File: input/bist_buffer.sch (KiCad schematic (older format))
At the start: 7 parts, among them U9 OPA1679

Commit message: Cleanup to get ready to start board layout. I had to get rid off all the bus signals, since in Kicad busses don't work that way.  Added a couple testpoints; many more needed.
Work on component placement in PCB.  I changed DGND to plain GND and "protective earth" to
"earth" (for chassis ground).  Chassis ground is now connected on the board only via a capacitor.
I had to fix the connector footprint to match the pin numbers on the symbol (there was a case
difference).
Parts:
- U9: footprint digikey-footprints:SOIC-14_W3.9mm -> Package_SO:SOIC-14_3.9x8.7mm_P1.27mm; symbol dk_Linear-Amplifiers-Instrumentation-OP-Amps-Buffer-Amps:LM324ADR -> ilemt_input:opamp_quad
- U9: footprint digikey-footprints:SOIC-14_W3.9mm -> Package_SO:SOIC-14_3.9x8.7mm_P1.27mm; symbol dk_Linear-Amplifiers-Instrumentation-OP-Amps-Buffer-Amps:LM324ADR -> ilemt_input:opamp_quad; Category (none) -> Integrated Circuits (ICs); DK_Datasheet_Link (none) -> http://www.ti.com/general/docs/suppproductinfo.tsp?distId=1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; DK_Detail_Page (none) -> /product-detail/en/texas-instruments/LM324ADR/296-9540-1-ND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; Description IC AUDIO 4 CIRCUIT 14SOIC -> IC OPAMP GP 4 CIRCUIT 14SOIC; Digi-Key_PN (none) -> 296-9540-1-ND; Family (none) -> Linear - Amplifiers - Instrumentation, OP Amps, Buffer Amps; MPN OPA1679IDR -> LM324ADR; Status (none) -> Active
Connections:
- net BIST++: no longer U9.2
- net BIST+-: no longer U9.6
- net BIST-+: no longer U9.9
- net BIST--: no longer U9.13
- new net BIST++_FB: U9.2
- new net BIST+-_FB: U9.6
- new net BIST-+_FB: U9.9
- new net BIST--_FB: U9.13
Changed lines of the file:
@@
 $EndDescr
 $Comp
-L dk_Linear-Amplifiers-Instrumentation-OP-Amps-Buffer-Amps:LM324ADR U9
+L ilemt_input:opamp_quad U9
 U 1 1 5E5A93B1
 P 4900 3100
 F 0 "U9" H 4600 3500 60  0000 C CNN
 F 1 "OPA1679" H 4350 3400 60  0000 L CNN
-F 2 "digikey-footprints:SOIC-14_W3.9mm" H 5100 3300 60  0001 L CNN
+F 2 "Package_SO:SOIC-14_3.9x8.7mm_P1.27mm" H 5100 3300 60  0001 L CNN
 F 3 "http://www.ti.com/general/docs/suppproductinfo.tsp?distId=10&gotoUrl=http%3A%2F%2Fwww.ti.com%2Flit%2Fgpn%2Fopa1679" H 5100 3400 60  0001 L CNN
 F 4 "OPA1679IDR" H 5100 3600 60  0001 L CNN "MPN"
@@
 	4900 3550 5150 3550
 Wire Wire Line
-	4900 2700 4900 2900
-Wire Wire Line
-	4900 3300 4900 3550
+	4900 2700 4900 2800
+Wire Wire Line
+	4900 3400 4900 3550
 $Comp
 L ilemt_input:V+ #PWR041
@@
 	4900 3700 4900 3550
 Connection ~ 4900 3550
-Text HLabel 2600 2150 0    50   Input ~ 0
-BIST_feedback
 Text GLabel 8300 3100 2    50   Input ~ 0
 BIST-+
@@
 Wire Wire Line
 	5550 3100 5200 3100
-Entry Wire Line
-	3900 2150 4000 2250
-Wire Wire Line
-	4000 2250 4000 3000
-Wire Wire Line
-	4000 3000 4600 3000
-Text Label 4050 3000 0    50   ~ 0
-BIST++
-$Comp
-L dk_Linear-Amplifiers-Instrumentation-OP-Amps-Buffer-Amps:LM324ADR U9
+$Comp
+L ilemt_input:opamp_quad U9
 U 2 1 5E5BA1D6
 P 7850 3100
 F 0 "U9" H 7550 3500 60  0000 C CNN
 F 1 "OPA1679" H 7300 3400 60  0000 L CNN
-F 2 "digikey-footprints:SOIC-14_W3.9mm" H 8050 3300 60  0001 L CNN
+F 2 "Package_SO:SOIC-14_3.9x8.7mm_P1.27mm" H 8050 3300 60  0001 L CNN
 F 3 "http://www.ti.com/general/docs/suppproductinfo.tsp?distId=10&gotoUrl=http%3A%2F%2Fwww.ti.com%2Flit%2Fgpn%2Fopa1679" H 8050 3400 60  0001 L CNN
-F 4 "OPA1679IDR" H 8050 3600 60  0001 L CNN "MPN"
-F 5 "IC AUDIO 4 CIRCUIT 14SOIC" H 8050 4100 60  0001 L CNN "Description"
+F 4 "LM324ADR" H 8050 3600 60  0001 L CNN "MPN"
+F 5 "IC OPAMP GP 4 CIRCUIT 14SOIC" H 8050 4100 60  0001 L CNN "Description"
 F 6 "Texas Instruments" H 8050 4200 60  0001 L CNN "Manufacturer"
 F 7 "296-46621-1-ND" H 7850 3100 50  0001 C CNN "Digikey"
+F 8 "Integrated Circuits (ICs)" H 7850 3100 50  0001 C CNN "Category"
+F 9 "http://www.ti.com/general/docs/suppproductinfo.tsp?distId=10&gotoUrl=http%3A%2F%2Fwww.ti.com%2Flit%2Fgpn%2Flm224" H 7850 3100 50  0001 C CNN "DK_Datasheet_Link"
+F 10 "/product-detail/en/texas-instruments/LM324ADR/296-9540-1-ND/405286" H 7850 3100 50  0001 C CNN "DK_Detail_Page"
+F 11 "296-9540-1-ND" H 7850 3100 50  0001 C CNN "Digi-Key_PN"
+F 12 "Linear - Amplifiers - Instrumentation, OP Amps, Buffer Amps" H 7850 3100 50  0001 C CNN "Family"
+F 13 "Active" H 7850 3100 50  0001 C CNN "Status"
 	2    7850 3100
 	1    0    0    -1
@@
 Wire Wire Line
 	8300 3100 8150 3100
-Entry Wire Line
-	6850 2150 6950 2250
-Wire Wire Line
-	6950 2250 6950 3000
-Wire Wire Line
-	6950 3000 7550 3000
-Text Label 7000 3000 0    50   ~ 0
-BIST+-
-$Comp
-L dk_Linear-Amplifiers-Instrumentation-OP-Amps-Buffer-Amps:LM324ADR U9
+$Comp
+L ilemt_input:opamp_quad U9
 U 3 1 5E5CB380
 P 4900 5050
 F 0 "U9" H 4600 5450 60  0000 C CNN
 F 1 "OPA1679" H 4350 5350 60  0000 L CNN
-F 2 "digikey-footprints:SOIC-14_W3.9mm" H 5100 5250 60  0001 L CNN
+F 2 "Package_SO:SOIC-14_3.9x8.7mm_P1.27mm" H 5100 5250 60  0001 L CNN
 F 3 "http://www.ti.com/general/docs/suppproductinfo.tsp?distId=10&gotoUrl=http%3A%2F%2Fwww.ti.com%2Flit%2Fgpn%2Fopa1679" H 5100 5350 60  0001 L CNN
-F 4 "OPA1679IDR" H 5100 5550 60  0001 L CNN "MPN"
-F 5 "IC AUDIO 4 CIRCUIT 14SOIC" H 5100 6050 60  0001 L CNN "Description"
+F 4 "LM324ADR" H 5100 5550 60  0001 L CNN "MPN"
+F 5 "IC OPAMP GP 4 CIRCUIT 14SOIC" H 5100 6050 60  0001 L CNN "Description"
 F 6 "Texas Instruments" H 5100 6150 60  0001 L CNN "Manufacturer"
 F 7 "296-46621-1-ND" H 4900 5050 50  0001 C CNN "Digikey"
+F 8 "Integrated Circuits (ICs)" H 4900 5050 50  0001 C CNN "Category"
+F 9 "http://www.ti.com/general/docs/suppproductinfo.tsp?distId=10&gotoUrl=http%3A%2F%2Fwww.ti.com%2Flit%2Fgpn%2Flm224" H 4900 5050 50  0001 C CNN "DK_Datasheet_Link"
+F 10 "/product-detail/en/texas-instruments/LM324ADR/296-9540-1-ND/405286" H 4900 5050 50  0001 C CNN "DK_Detail_Page"
+F 11 "296-9540-1-ND" H 4900 5050 50  0001 C CNN "Digi-Key_PN"
+F 12 "Linear - Amplifiers - Instrumentation, OP Amps, Buffer Amps" H 4900 5050 50  0001 C CNN "Family"
+F 13 "Active" H 4900 5050 50  0001 C CNN "Status"
 	3    4900 5050
 	1    0    0    -1
@@
 Wire Wire Line
 	5550 5050 5200 5050
-Entry Wire Line
-	3900 4100 4000 4200
-Wire Wire Line
-	4000 4200 4000 4950
-Wire Wire Line
-	4000 4950 4600 4950
-Text Label 4050 4950 0    50   ~ 0
-BIST-+
-$Comp
-L dk_Linear-Amplifiers-Instrumentation-OP-Amps-Buffer-Amps:LM324ADR U9
+$Comp
+L ilemt_input:opamp_quad U9
 U 4 1 5E5CB3CA
 P 7850 5050
 F 0 "U9" H 7550 5450 60  0000 C CNN
 F 1 "OPA1679" H 7300 5350 60  0000 L CNN
-F 2 "digikey-footprints:SOIC-14_W3.9mm" H 8050 5250 60  0001 L CNN
+F 2 "Package_SO:SOIC-14_3.9x8.7mm_P1.27mm" H 8050 5250 60  0001 L CNN
 F 3 "http://www.ti.com/general/docs/suppproductinfo.tsp?distId=10&gotoUrl=http%3A%2F%2Fwww.ti.com%2Flit%2Fgpn%2Fopa1679" H 8050 5350 60  0001 L CNN
 F 4 "OPA1679IDR" H 8050 5550 60  0001 L CNN "MPN"
@@
 Wire Wire Line
 	8300 5050 8150 5050
-Entry Wire Line
-	6850 4100 6950 4200
-Wire Wire Line
-	6950 4200 6950 4950
-Wire Wire Line
-	6950 4950 7550 4950
-Text Label 7000 4950 0    50   ~ 0
-BIST--
 $Comp
 L ilemt_input:V- #PWR042
@@
 	1    0    0    -1
 $EndComp
-Wire Bus Line
-	2950 4100 2950 2150
-Wire Bus Line
-	2600 2150 2950 2150
-Connection ~ 2950 2150
 Text Notes 7100 6850 0    50   ~ 0
 BIST buffer\nBuffers the Built In Self Test signals from the main board, using feedback\nfrom channel 1 to null out the diode drop.
 Text Notes 7400 4350 0    50   ~ 0
 The BIST buffer is in effect a "precision rectifier" because the outputs are thru\ndiodes and the feedback is taken after the diode.  This cancels the diode Vf.\nThe diodes are placed at the input of each channel, with all channels in \nparallel.  The feedback can only be taken from a single channel (channel 1),\nso the Vf cancellation on the other channels depends on diode matching.\n\nDuring normal operation the input BIST lines are set at 0V for BIST?+\nand 5V for BIST?-.  This causes the BIST buffer to saturate at V+ or V- \nso as to reverse-bias the injection diodes.
-Wire Bus Line
-	2950 4100 6850 4100
-Wire Bus Line
-	2950 2150 6850 2150
+Text GLabel 6750 3000 0    50   Input ~ 0
+BIST+-_FB
+Wire Wire Line
+	6750 3000 7550 3000
+Text GLabel 3800 3000 0    50   Input ~ 0
+BIST++_FB
+Wire Wire Line
+	3800 3000 4600 3000
+Text GLabel 3800 4950 0    50   Input ~ 0
+BIST-+_FB
+Wire Wire Line
+	3800 4950 4600 4950
+Text GLabel 6750 4950 0    50   Input ~ 0
+BIST--_FB
+Wire Wire Line
+	6750 4950 7550 4950
 $EndSCHEMATC

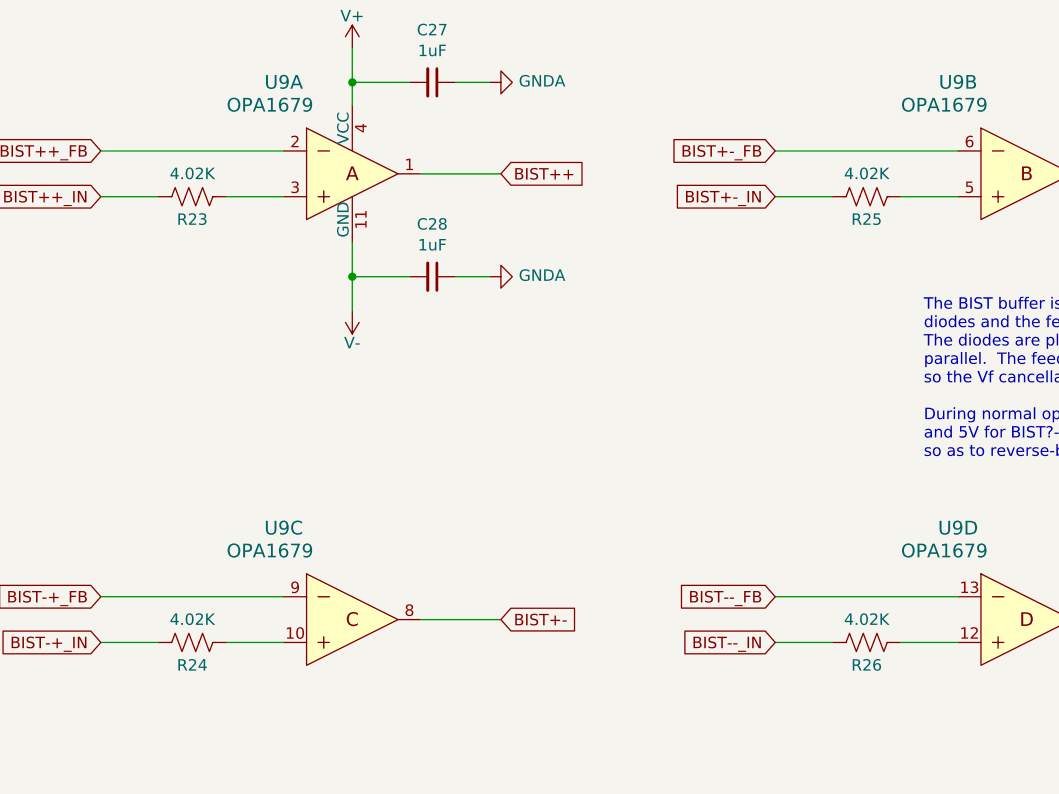
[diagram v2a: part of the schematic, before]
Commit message: Changed board connector to PCIe 8x, added test points, cleanup of component values. Add LVDS Rx termination, bypass caps.
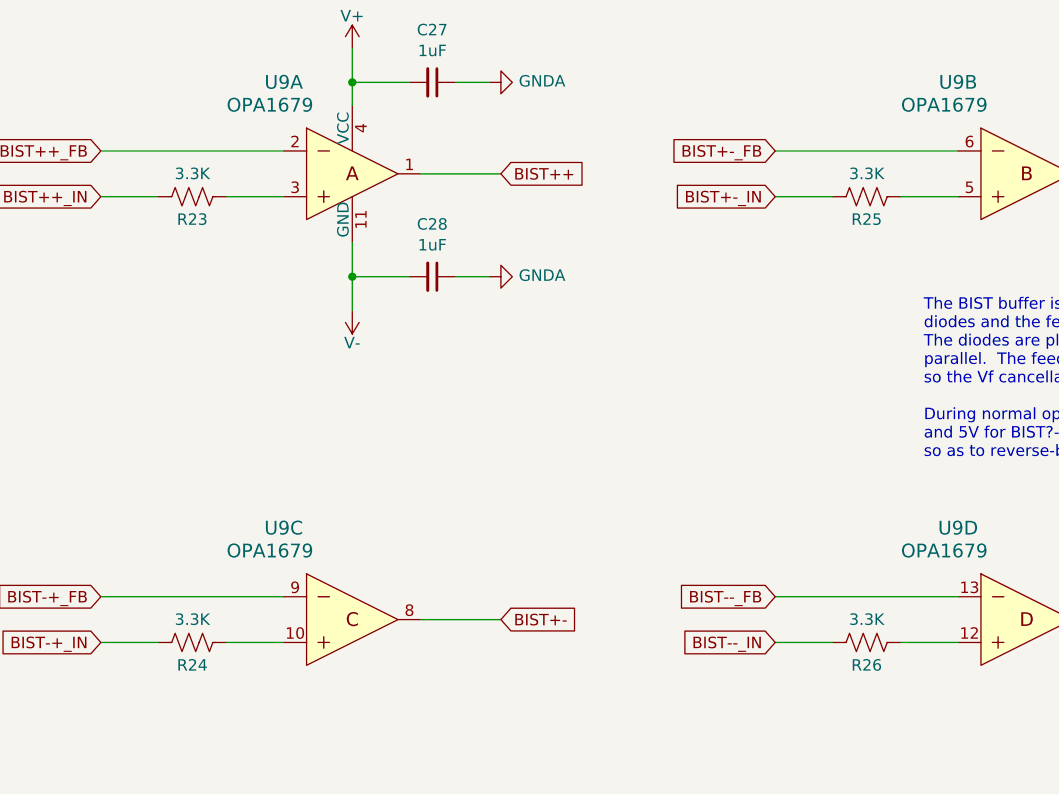
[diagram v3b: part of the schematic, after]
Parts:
- R23, R24, R25, R26: value 4.02K -> 3.3K; footprint Resistor_SMD:R_0805_2012Metric -> Resistor_SMD:R_0603_1608Metric
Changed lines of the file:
@@
 AR Path="/5E5A51EB/5E5B741A" Ref="R23"  Part="1"
 F 0 "R23" V 4300 3200 50  0000 C CNN
-F 1 "4.02K" V 4100 3200 50  0000 C CNN
-F 2 "Resistor_SMD:R_0805_2012Metric" V 4240 3190 50  0001 C CNN
+F 1 "3.3K" V 4100 3200 50  0000 C CNN
+F 2 "Resistor_SMD:R_0603_1608Metric" V 4240 3190 50  0001 C CNN
 F 3 "~" H 4200 3200 50  0001 C CNN
 F 4 "0.1%" H 4200 3200 50  0001 C CNN "Notes"
@@
 AR Path="/5E5A51EB/5E5BA20D" Ref="R25"  Part="1"
 F 0 "R25" V 7250 3200 50  0000 C CNN
-F 1 "4.02K" V 7050 3200 50  0000 C CNN
-F 2 "Resistor_SMD:R_0805_2012Metric" V 7190 3190 50  0001 C CNN
+F 1 "3.3K" V 7050 3200 50  0000 C CNN
+F 2 "Resistor_SMD:R_0603_1608Metric" V 7190 3190 50  0001 C CNN
 F 3 "~" H 7150 3200 50  0001 C CNN
 F 4 "0.1%" H 7150 3200 50  0001 C CNN "Notes"
@@
 AR Path="/5E5A51EB/5E5CB3B9" Ref="R24"  Part="1"
 F 0 "R24" V 4300 5150 50  0000 C CNN
-F 1 "4.02K" V 4100 5150 50  0000 C CNN
-F 2 "Resistor_SMD:R_0805_2012Metric" V 4240 5140 50  0001 C CNN
+F 1 "3.3K" V 4100 5150 50  0000 C CNN
+F 2 "Resistor_SMD:R_0603_1608Metric" V 4240 5140 50  0001 C CNN
 F 3 "~" H 4200 5150 50  0001 C CNN
 F 4 "0.1%" H 4200 5150 50  0001 C CNN "Notes"
@@
 AR Path="/5E5A51EB/5E5CB3D1" Ref="R26"  Part="1"
 F 0 "R26" V 7250 5150 50  0000 C CNN
-F 1 "4.02K" V 7050 5150 50  0000 C CNN
-F 2 "Resistor_SMD:R_0805_2012Metric" V 7190 5140 50  0001 C CNN
+F 1 "3.3K" V 7050 5150 50  0000 C CNN
+F 2 "Resistor_SMD:R_0603_1608Metric" V 7190 5140 50  0001 C CNN
 F 3 "~" H 7150 5150 50  0001 C CNN
 F 4 "0.1%" H 7150 5150 50  0001 C CNN "Notes"
